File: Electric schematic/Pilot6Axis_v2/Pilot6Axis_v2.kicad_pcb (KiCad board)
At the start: 2 copper layers, 171 x 83.9 mm, 125 parts, among them IC1 LM27313XMFX_NOPB, IC2 TPS25751SRSMR, IC3 BQ25792RQMR, IC4 TPS3422EGDRYR, IC5 SN74LVC1G74RSE2, J1 Battery input, J10 Conn_01x06, J3 USB_C_Receptacle_USB2.0_16P, J4 Conn_01x06, J6 Oled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

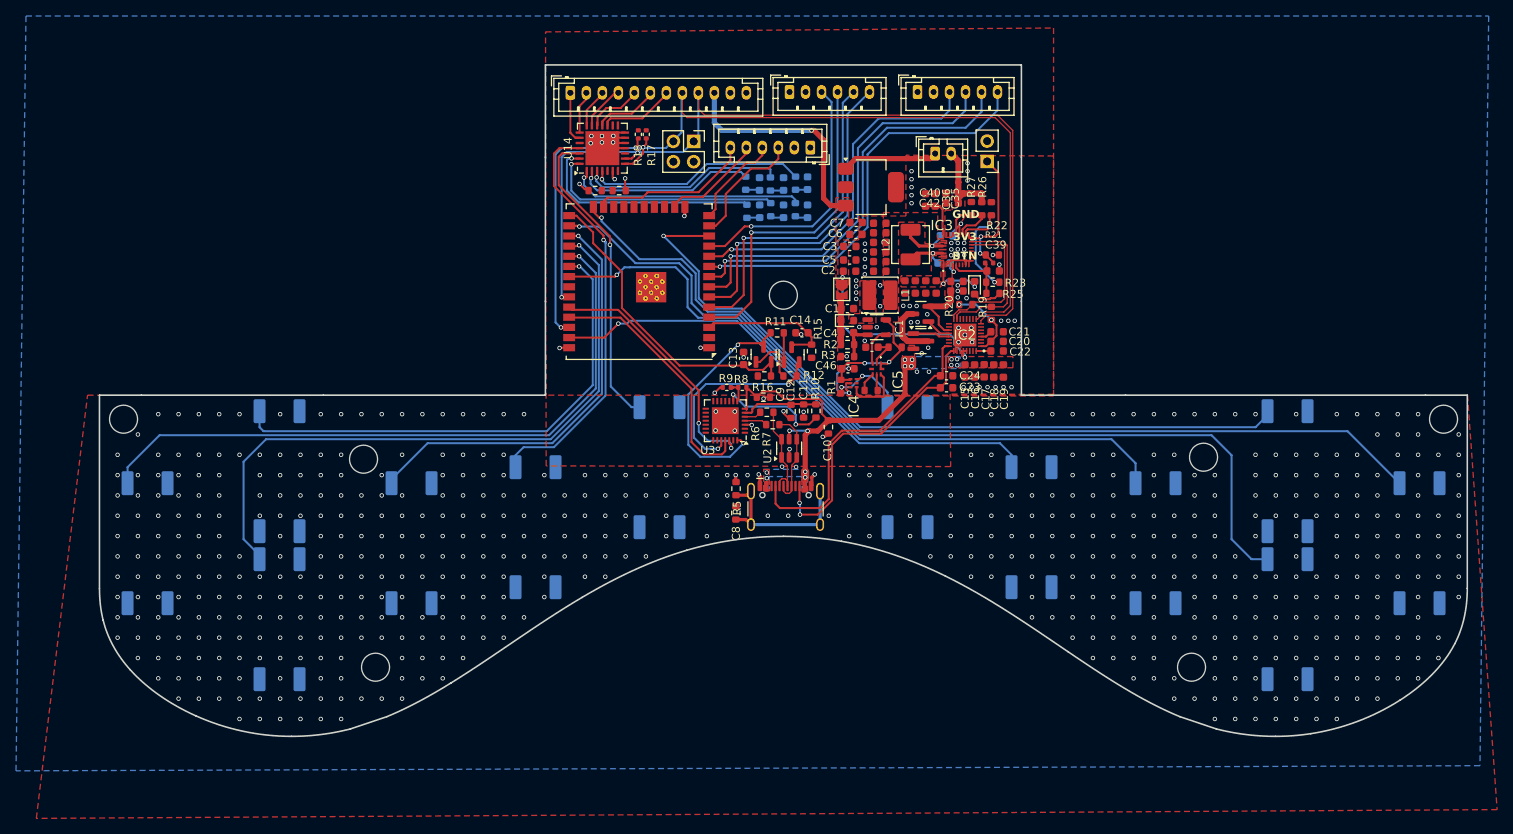
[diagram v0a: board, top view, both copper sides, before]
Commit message: [pcb] added eeprom to pd charger so the ciofnig is remembered and set correctly
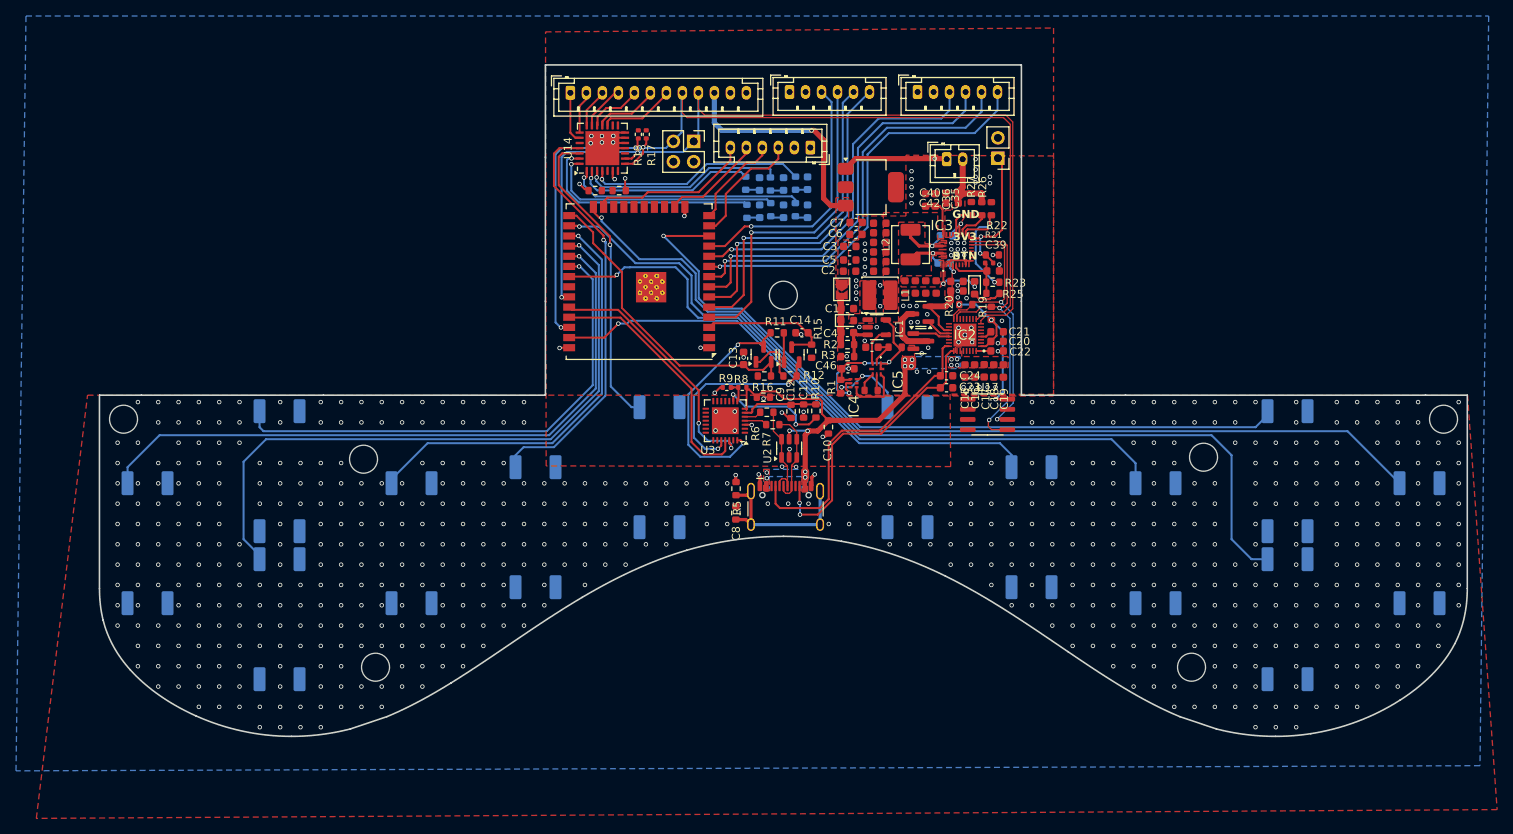
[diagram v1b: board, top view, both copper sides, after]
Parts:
- added U17: CAT24C512WI-GT3, Package_SO:SOIC-8_3.9x4.9mm_P1.27mm, F.Cu at (178.6, 106.0)
- moved J1 1.61 mm to (173.5, 74.1)
- moved TH1 1.41 mm to (179.9, 74.0)
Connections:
- IC2 pad 28: +5V -> unconnected-(IC2-PP5V_1-Pad28)
- IC2 pad 29: +5V -> unconnected-(IC2-PP5V_2-Pad29)
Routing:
- net +5V: track 53.5 -> 28.7 mm, vias 3 -> 1
- net /PD/I2CC_SDA: track 19.3 -> 38.9 mm, vias 0 -> 2
- net /PD/I2CC_SCL: track 18.4 -> 35.8 mm, vias 0 -> 2
- net /PD/LDO_3V3: track 9.60 -> 22.0 mm, vias 2 -> 3
- net GND: track 48.9 -> 50.1 mm, vias 687 -> 729
- net /GPIO/SDA: track 115.6 -> 116.2 mm
- net /GPIO/SCL: track 121.1 -> 121.7 mm
- net /BAT+: track 9.90 -> 9.30 mm
